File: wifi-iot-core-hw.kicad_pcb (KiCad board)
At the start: 2 copper layers, 28.4 x 58.4 mm, 52 parts, among them P1 CONN_01X20, P2 CONN_01X20, P3 CONN_01X01, P4 CONN_01X01, P5 CONN_01X01, P6 CONN_01X01, P7 CONN_01X04, P8 USB, SW1 RST, SW2 SW_PUSH_SMALL_H, U1 ESP-07v2, U2 STM32F103C8Tx, U3 LP2985LV, Y1 8MHz, Y2 32.687

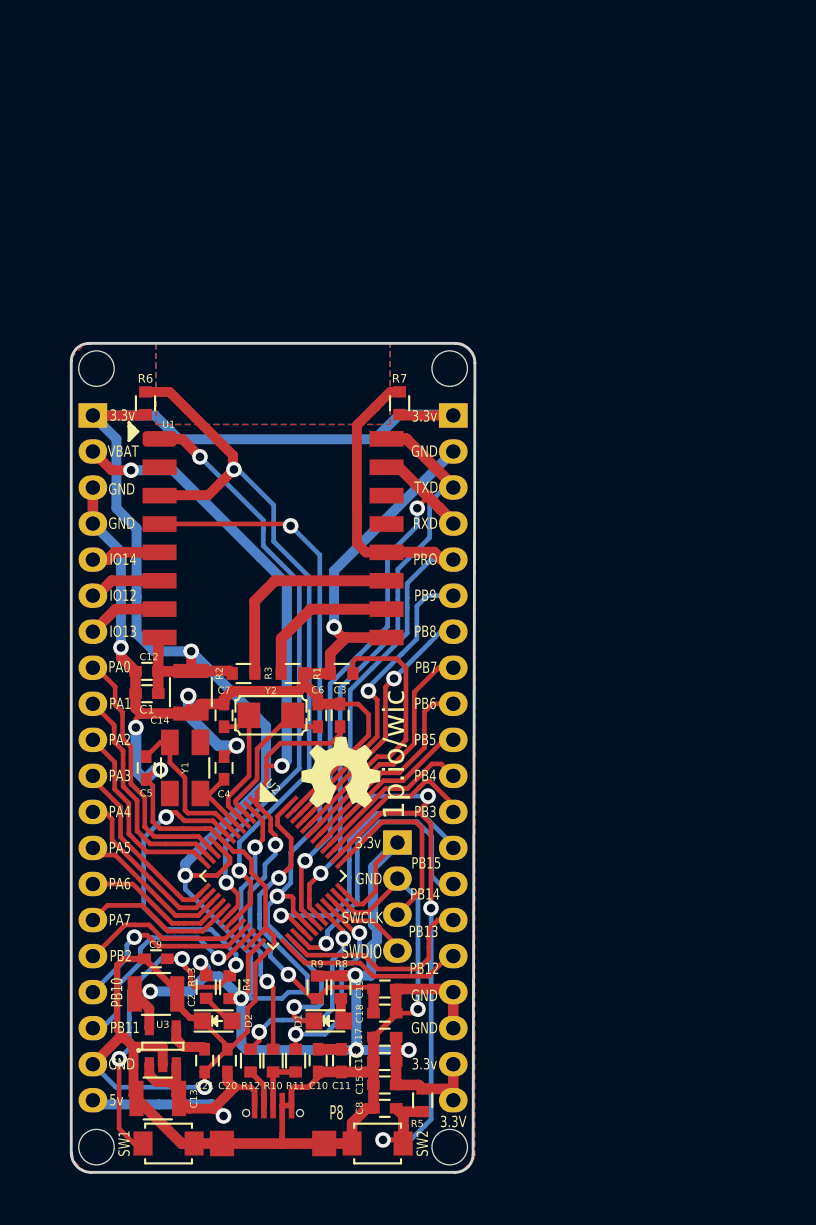
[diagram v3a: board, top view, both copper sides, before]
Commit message: Drop pin GPIO16 at pin STM32, add address support in PCB & size PCB 2,3x1,25 inch (5,8x3,2 mm)
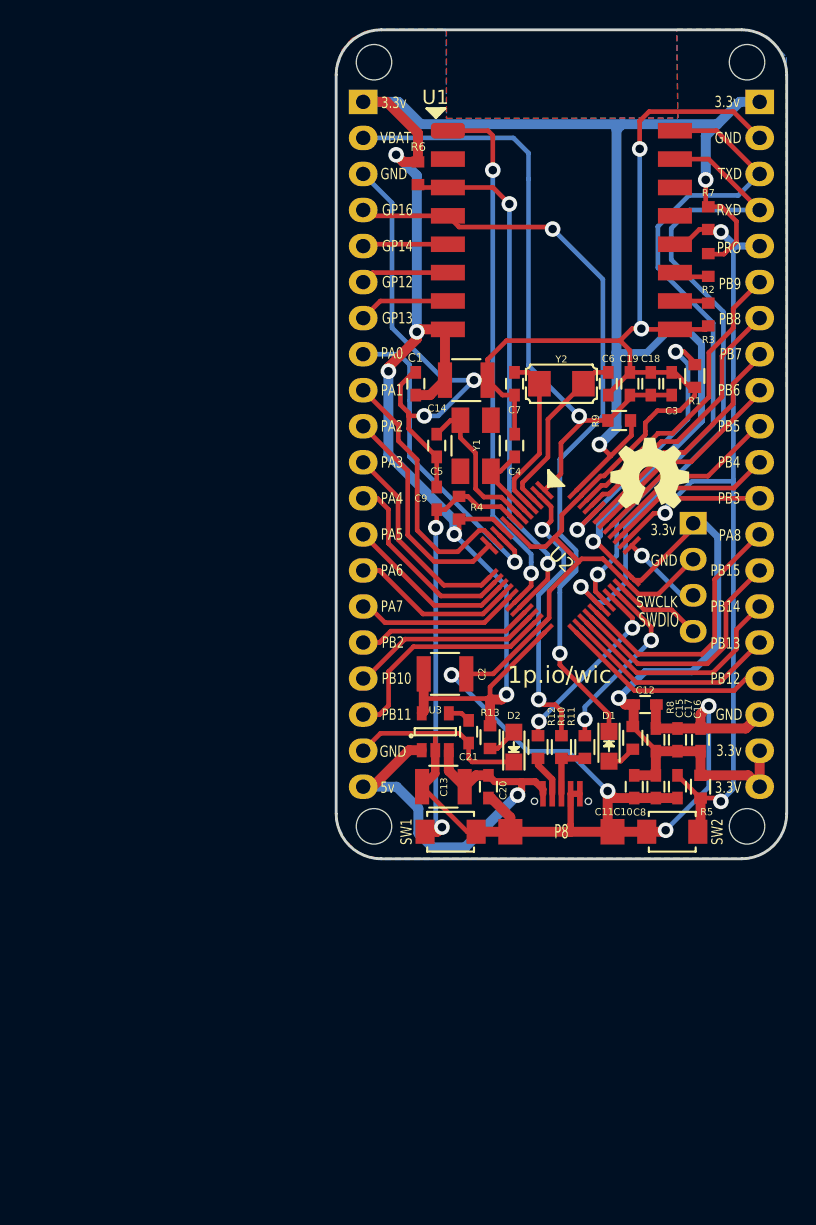
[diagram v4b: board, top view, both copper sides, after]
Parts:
- moved C18 48.2 mm to (148.5, 79.0), turned to 270 degrees
- moved C19 46.0 mm to (147.1, 79.0), turned to 270 degrees
- moved R9 45.3 mm to (146.3, 81.6), turned to 0 degrees
- moved R2 43.6 mm to (152.6, 70.7), turned to 270 degrees
- moved R3 38.7 mm to (152.6, 74.2), turned to 270 degrees
- moved C9 38.0 mm to (133.5, 87.1), turned to 90 degrees
- moved R4 37.5 mm to (135.0, 87.8)
- moved C12 35.2 mm to (148.1, 101.7), turned to 0 degrees
- moved C3 33.0 mm to (150.0, 79.0)
- moved R1 32.5 mm to (151.6, 78.5), turned to 270 degrees
- moved C16 31.8 mm to (152.0, 104.1), turned to 270 degrees
- moved C6 31.1 mm to (145.5, 79.0), turned to 270 degrees
- moved Y2 31.1 mm to (142.2, 79.0)
- moved C7 31.1 mm to (138.9, 79.0), turned to 270 degrees
- moved C15 30.9 mm to (148.9, 104.1), turned to 270 degrees
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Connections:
- P1 pad 4: GNDREF -> /GPIO16
- P2 pad 13: PB15 -> PA8
- P2 pad 14: PB14 -> PB15
- P2 pad 15: PB13 -> PB14
- P2 pad 16: PB12 -> PB13
- P2 pad 17: GNDREF -> PB12
- U2 pad 29: /GPIO16 -> PA8
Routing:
- net +3V3: track 207.3 -> 245.1 mm
- net /VBAT: track 80.9 -> 45.9 mm, vias 4 -> 1
- net /ESP_PRO: track 86.6 -> 62.8 mm
- net PA8: track 0.00 -> 18.8 mm
- net /CH_PD: track 52.3 -> 37.4 mm
- net /RST: track 45.6 -> 31.1 mm, vias 4 -> 2
- net Net-(R2-Pad2): track 15.0 -> 2.29 mm
- net /ESP_RXD: track 41.0 -> 49.8 mm, vias 2 -> 1
- net Net-(R3-Pad1): track 10.7 -> 2.22 mm
- net /SWCLK: track 13.6 -> 5.79 mm, vias 0 -> 1
- net /ESP_RST: track 44.9 -> 37.8 mm
- net /ESP_TXD: track 41.9 -> 47.8 mm
- net +5V: track 26.6 -> 31.7 mm
- net PB14: track 21.5 -> 16.4 mm, vias 1 -> 0
- net PA0: track 18.3 -> 22.9 mm, vias 0 -> 1
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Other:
- board size 28.4 x 58.4 mm -> 31.8 x 58.4 mm
- board text added: "GP12"
- board text added: "GP13"
- board text added: "GP14"
- board text added: "GP16"
- board text added: "PA8"
- board text removed: "IO12"
- board text removed: "IO13"
- board text removed: "IO14"

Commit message: Fix assets file
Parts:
- moved R7 0.20 mm to (152.6, 67.2)
- renumbered SW2 to PRO, SW1 to RST
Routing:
- net +3V3: track 245.1 -> 237.4 mm
- net /ESP_PRO: track 62.8 -> 63.7 mm
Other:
- net class Default: clearance 0.1 -> 0.254
- rule trace_clearance: 0.1 -> 0.254
